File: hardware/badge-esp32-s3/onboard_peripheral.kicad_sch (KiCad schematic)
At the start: 0 parts

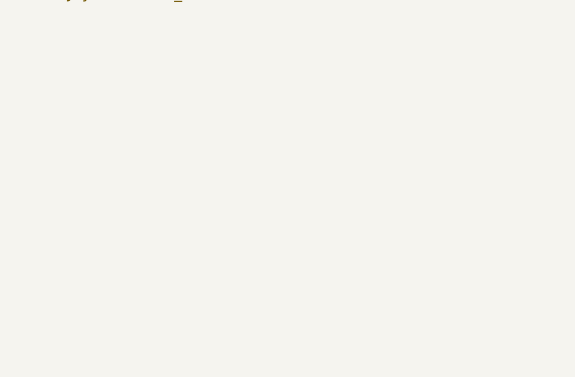
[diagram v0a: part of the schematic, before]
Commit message: Accelerometer
I Ended up doing just the accelerometer, the others would have taken more pins etc.
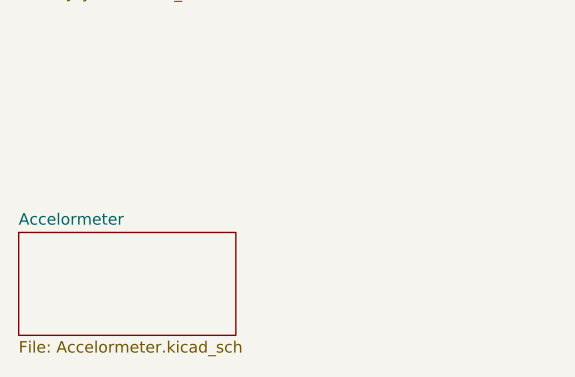
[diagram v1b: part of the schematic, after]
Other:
- added sheet Accelormeter (Accelormeter.kicad_sch)
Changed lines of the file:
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@@
+	)
+	(sheet
+		(at 53.34 153.67)
+		(size 24.13 11.43)
+		(exclude_from_sim no)
+		(in_bom yes)
+		(on_board yes)
+		(dnp no)
+		(fields_autoplaced yes)
+		(stroke
+			(width 0.1524)
+			(type solid)
+		)
+		(fill
+			(color 0 0 0 0.0000)
+		)
+		(property "Sheetname" "Accelormeter"
+			(at 53.34 152.9584 0)
+			(effects
+				(font
+					(size 1.27 1.27)
+				)
+				(justify left bottom)
+			)
+		)
+		(property "Sheetfile" "Accelormeter.kicad_sch"
+			(at 53.34 165.6846 0)
+			(effects
+				(font
+					(size 1.27 1.27)
+				)
+				(justify left top)
+			)
+		)
+		(instances
+			(project "badge-esp32-s3"
+				(path "/e2af9a6c-dbe9-4de2-9ba6-ea213a7300ec/9feb22ac-0492-47b5-89fe-3e77a54de168"
+					(page "22")
+				)
+			)
+		)
 	)
 	(sheet

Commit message: Revert "Merge branch 'main' into Danny"
This reverts commit f39a0d75d6025751b3d0be32cc251741b689ee9f, reversing
changes made to 38c8f4414de6e086c66d277d9ce522e64904a3dc.
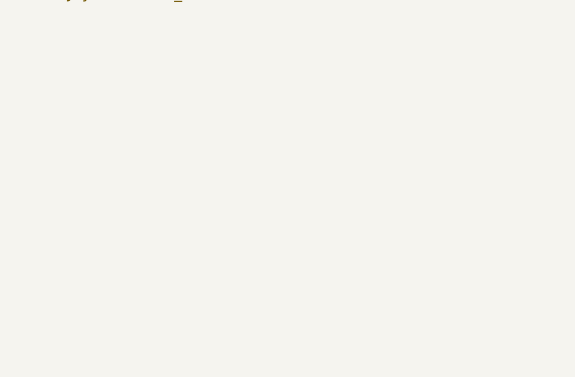
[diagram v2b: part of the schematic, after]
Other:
- removed sheet Accelormeter
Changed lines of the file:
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@@
-	)
-	(sheet
-		(at 53.34 153.67)
-		(size 24.13 11.43)
-		(exclude_from_sim no)
-		(in_bom yes)
-		(on_board yes)
-		(dnp no)
-		(fields_autoplaced yes)
-		(stroke
-			(width 0.1524)
-			(type solid)
-		)
-		(fill
-			(color 0 0 0 0.0000)
-		)
-		(property "Sheetname" "Accelormeter"
-			(at 53.34 152.9584 0)
-			(effects
-				(font
-					(size 1.27 1.27)
-				)
-				(justify left bottom)
-			)
-		)
-		(property "Sheetfile" "Accelormeter.kicad_sch"
-			(at 53.34 165.6846 0)
-			(effects
-				(font
-					(size 1.27 1.27)
-				)
-				(justify left top)
-			)
-		)
-		(instances
-			(project "badge-esp32-s3"
-				(path "/e2af9a6c-dbe9-4de2-9ba6-ea213a7300ec/9feb22ac-0492-47b5-89fe-3e77a54de168"
-					(page "22")
-				)
-			)
-		)
 	)
 	(sheet
